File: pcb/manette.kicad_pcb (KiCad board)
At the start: 2 copper layers, 95 x 51.5 mm, 13 parts

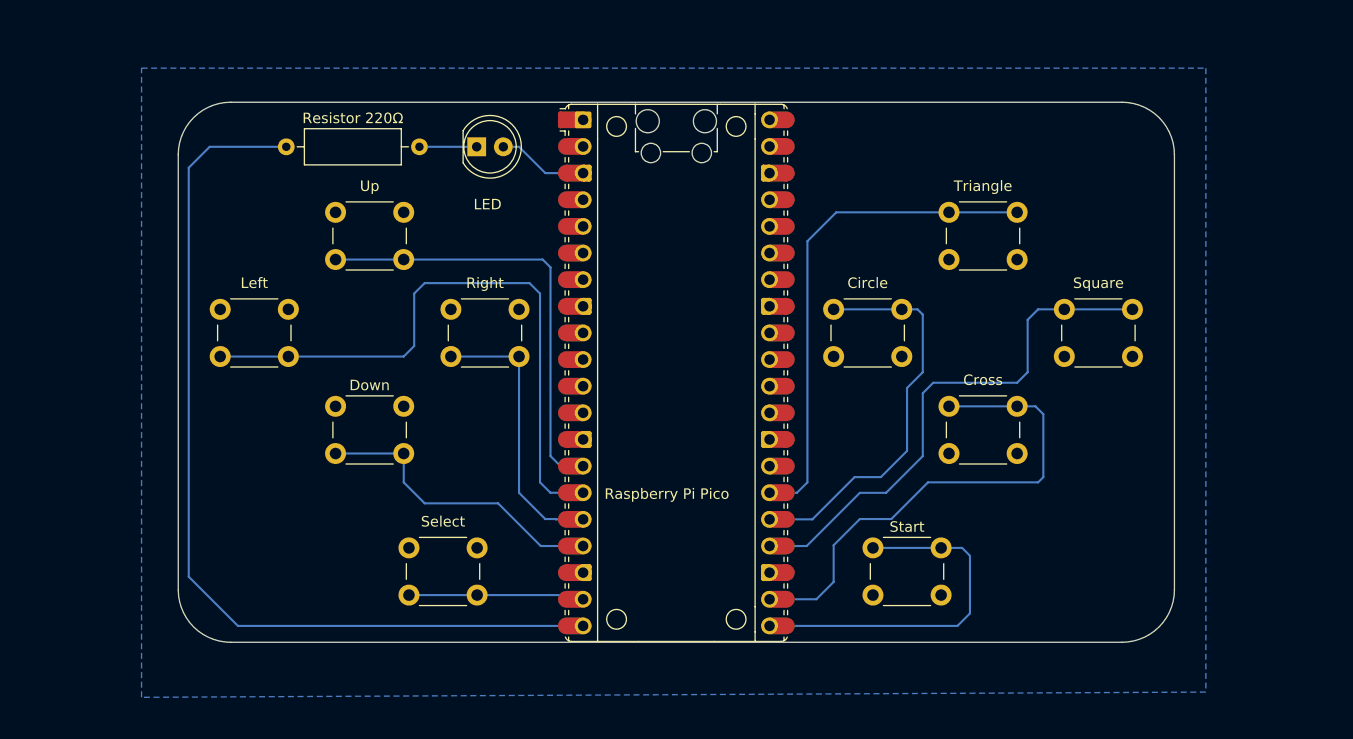
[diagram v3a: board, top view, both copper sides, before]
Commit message: ajout trous de fixation, élargissement des pistes et des pads
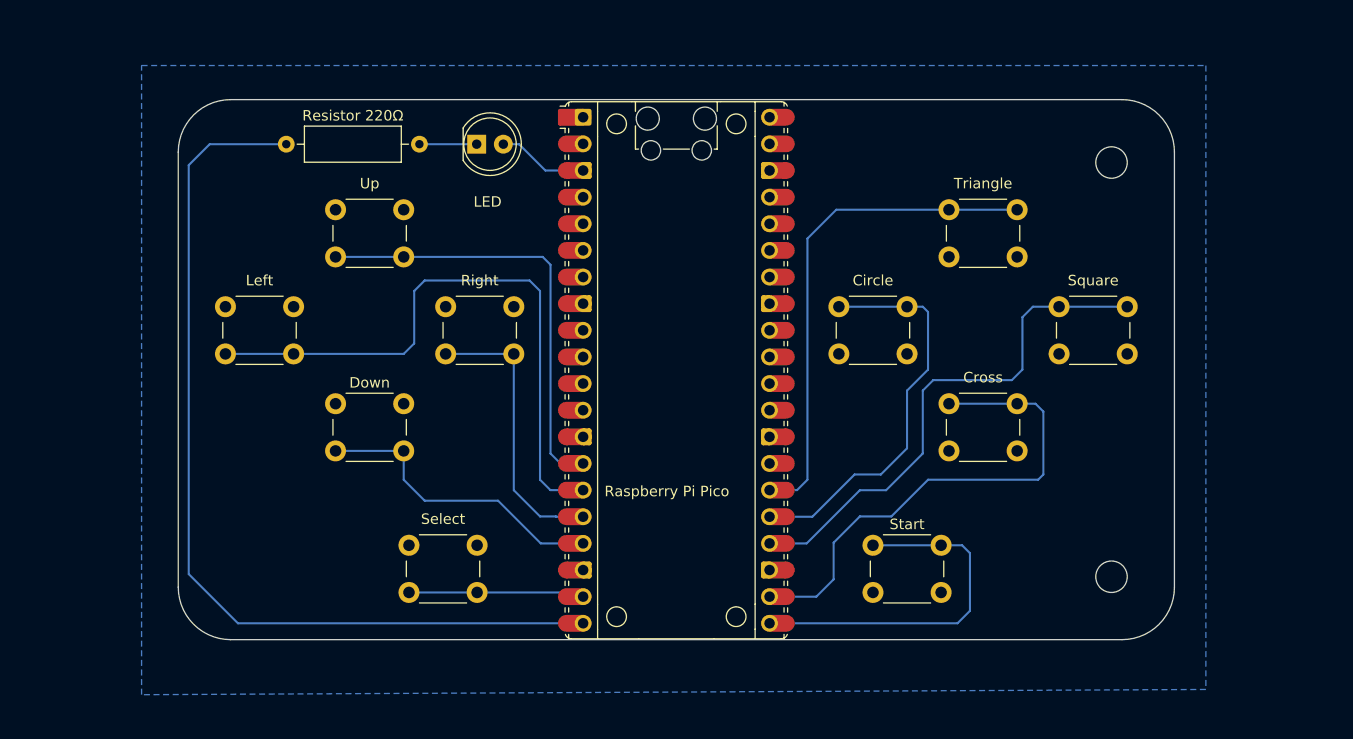
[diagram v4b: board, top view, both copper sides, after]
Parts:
- moved Circle 0.56 mm to (165.5, 98.8)
- moved Left 0.56 mm to (107.0, 98.8)
- moved Right 0.56 mm to (128.0, 98.8)
- moved Square 0.56 mm to (186.5, 98.8)
- moved Cross 0.25 mm to (176.0, 108.0)
- moved Down 0.25 mm to (117.5, 108.0)
- moved LED 0.25 mm to (131.0, 83.2)
- moved Raspberry Pi Pico 0.25 mm to (150.0, 104.8)
- moved Resistor 220Ω 0.25 mm to (112.8, 83.2)
- moved Select 0.25 mm to (124.5, 121.5)
- moved Start 0.25 mm to (168.8, 121.5)
- moved Triangle 0.25 mm to (176.0, 89.5)
- moved Up 0.25 mm to (117.5, 89.5)
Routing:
- net Net-(A1-GPIO18): track 50.4 -> 49.9 mm
- net Net-(A1-GPIO12): track 26.7 -> 27.2 mm
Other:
- outline, holes or cut-outs redrawn

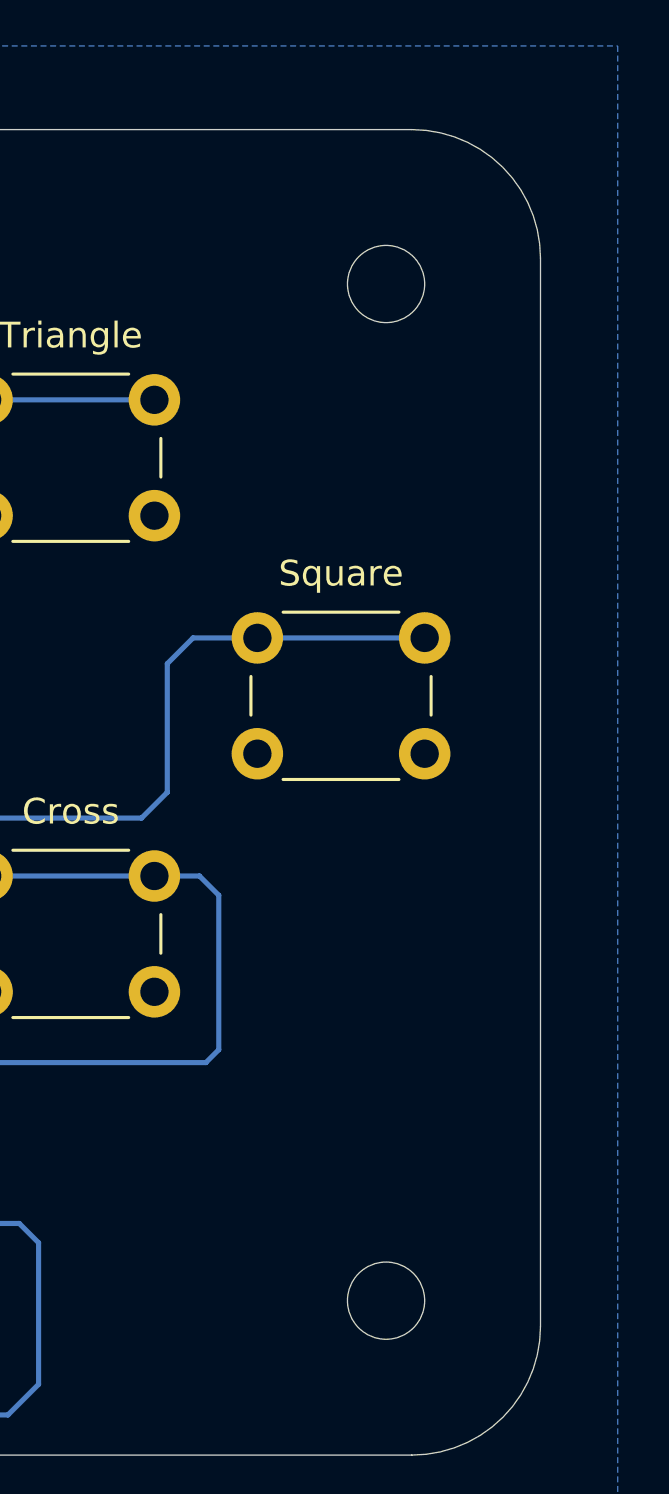
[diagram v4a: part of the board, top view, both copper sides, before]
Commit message: replaced edge.cut holes with footprint drill holes
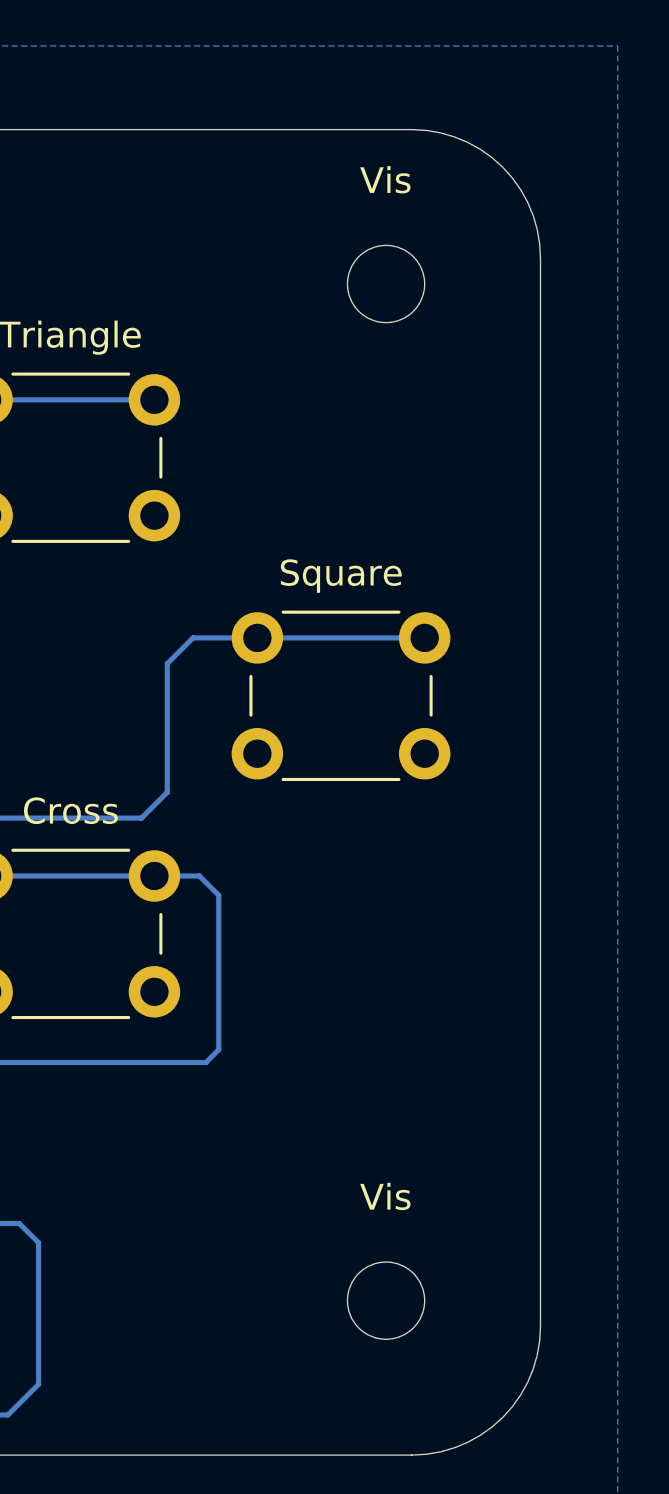
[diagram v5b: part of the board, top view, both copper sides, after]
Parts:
- added Vis: MountingHole_3mm, MountingHole:MountingHole_3mm, F.Cu at (191.5, 124.5)
- added Vis: MountingHole_3mm, MountingHole:MountingHole_3mm, F.Cu at (191.5, 85.0)
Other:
- outline, holes or cut-outs redrawn
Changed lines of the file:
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@@
 	(net 56 "unconnected-(A1-3V3_EN-Pad37)_1")
 	(net 57 "Net-(D1-K)")
+	(footprint "MountingHole:MountingHole_3mm"
+		(layer "F.Cu")
+		(at 191.5 124.5)
+		(descr "Mounting Hole 3mm, no annular")
+		(tags "mounting hole 3mm no annular")
+		(property "Reference" "Vis"
+			(at 0 -4 0)
+			(layer "F.SilkS")
+			(effects
+				(font
+					(size 1 1)
+					(thickness 0.15)
+				)
+			)
+		)
+		(property "Value" "MountingHole_3mm"
+			(at 0 4 0)
+			(layer "F.Fab")
+			(effects
+				(font
+					(size 1 1)
+					(thickness 0.15)
+				)
+			)
+		)
+		(property "Footprint" "MountingHole:MountingHole_3mm"
+			(at 0 0 0)
+			(unlocked yes)
+			(layer "F.Fab")
+			(hide yes)
+			(effects
+				(font
+					(size 1.27 1.27)
+					(thickness 0.15)
+				)
+			)
+		)
+		(property "Datasheet" ""
+			(at 0 0 0)
+			(unlocked yes)
+			(layer "F.Fab")
+			(hide yes)
+			(effects
+				(font
+					(size 1.27 1.27)
+					(thickness 0.15)
+				)
+			)
+		)
+		(property "Description" ""
+			(at 0 0 0)
+			(unlocked yes)
+			(layer "F.Fab")
+			(hide yes)
+			(effects
+				(font
+					(size 1.27 1.27)
+					(thickness 0.15)
+				)
+			)
+		)
+		(attr exclude_from_pos_files exclude_from_bom)
+		(fp_circle
+			(center 0 0)
+			(end 3 0)
+			(stroke
+				(width 0.15)
+				(type solid)
+			)
+			(fill none)
+			(layer "Cmts.User")
+		)
+		(fp_circle
+			(center 0 0)
+			(end 3.25 0)
+			(stroke
+				(width 0.05)
+				(type solid)
+			)
+			(fill none)
+			(layer "F.CrtYd")
+		)
+		(fp_text user "${REFERENCE}"
+			(at 0 0 0)
+			(layer "F.Fab")
+			(effects
+				(font
+					(size 1 1)
+					(thickness 0.15)
+				)
+			)
+		)
+		(pad "" np_thru_hole circle
+			(at 0 0)
+			(size 3 3)
+			(drill 3)
+			(layers "*.Cu" "*.Mask" "In1.Cu" "In2.Cu" "In3.Cu" "In4.Cu" "In5.Cu" "In6.Cu"
+				"In7.Cu" "In8.Cu" "In9.Cu" "In10.Cu" "In11.Cu" "In12.Cu" "In13.Cu" "In14.Cu"
+				"In15.Cu" "In16.Cu" "In17.Cu" "In18.Cu" "In19.Cu" "In20.Cu" "In21.Cu"
+				"In22.Cu" "In23.Cu" "In24.Cu" "In25.Cu" "In26.Cu" "In27.Cu" "In28.Cu"
+				"In29.Cu" "In30.Cu"
+			)
+		)
+	)
 	(footprint "Button_Switch_THT:SW_PUSH_6mm_H4.3mm"
 		(layer "F.Cu")
@@
 		)
 	)
+	(footprint "MountingHole:MountingHole_3mm"
+		(layer "F.Cu")
+		(at 191.5 85)
+		(descr "Mounting Hole 3mm, no annular")
+		(tags "mounting hole 3mm no annular")
+		(property "Reference" "Vis"
+			(at 0 -4 0)
+			(layer "F.SilkS")
+			(effects
+				(font
+					(size 1 1)
+					(thickness 0.15)
+				)
+			)
+		)
+		(property "Value" "MountingHole_3mm"
+			(at 0 4 0)
+			(layer "F.Fab")
+			(effects
+				(font
+					(size 1 1)
+					(thickness 0.15)
+				)
+			)
+		)
+		(property "Footprint" "MountingHole:MountingHole_3mm"
+			(at 0 0 0)
+			(unlocked yes)
+			(layer "F.Fab")
+			(hide yes)
+			(effects
+				(font
+					(size 1.27 1.27)
+					(thickness 0.15)
+				)
+			)
+		)
+		(property "Datasheet" ""
+			(at 0 0 0)
+			(unlocked yes)
+			(layer "F.Fab")
+			(hide yes)
+			(effects
+				(font
+					(size 1.27 1.27)
+					(thickness 0.15)
+				)
+			)
+		)
+		(property "Description" ""
+			(at 0 0 0)
+			(unlocked yes)
+			(layer "F.Fab")
+			(hide yes)
+			(effects
+				(font
+					(size 1.27 1.27)
+					(thickness 0.15)
+				)
+			)
+		)
+		(attr exclude_from_pos_files exclude_from_bom)
+		(fp_circle
+			(center 0 0)
+			(end 3 0)
+			(stroke
+				(width 0.15)
+				(type solid)
+			)
+			(fill none)
+			(layer "Cmts.User")
+		)
+		(fp_circle
+			(center 0 0)
+			(end 3.25 0)
+			(stroke
+				(width 0.05)
+				(type solid)
+			)
+			(fill none)
+			(layer "F.CrtYd")
+		)
+		(fp_text user "${REFERENCE}"
+			(at 0 0 0)
+			(layer "F.Fab")
+			(effects
+				(font
+					(size 1 1)
+					(thickness 0.15)
+				)
+			)
+		)
+		(pad "" np_thru_hole circle
+			(at 0 0)
+			(size 3 3)
+			(drill 3)
+			(layers "*.Cu" "*.Mask" "In1.Cu" "In2.Cu" "In3.Cu" "In4.Cu" "In5.Cu" "In6.Cu"
+				"In7.Cu" "In8.Cu" "In9.Cu" "In10.Cu" "In11.Cu" "In12.Cu" "In13.Cu" "In14.Cu"
+				"In15.Cu" "In16.Cu" "In17.Cu" "In18.Cu" "In19.Cu" "In20.Cu" "In21.Cu"
+				"In22.Cu" "In23.Cu" "In24.Cu" "In25.Cu" "In26.Cu" "In27.Cu" "In28.Cu"
+				"In29.Cu" "In30.Cu"
+			)
+		)
+	)
 	(footprint "Button_Switch_THT:SW_PUSH_6mm_H4.3mm"
 		(layer "F.Cu")
@@
 		(tags "Resistor Axial_DIN0309 series Axial Horizontal pin pitch 12.7mm 0.5W = 1/2W length 9mm diameter 3.2mm")
 		(property "Reference" "Resistor 220Ω"
-			(at 6.35 -2.72 360)
+			(at 6.35 -2.72 0)
 			(layer "F.SilkS")
 			(effects
@@
 		)
 		(property "Value" "220Ω"
-			(at 6.35 2.72 360)
+			(at 6.35 2.72 0)
 			(layer "F.Fab")
 			(effects
@@
 		)
 		(fp_text user "${REFERENCE}"
-			(at 6.35 0 360)
+			(at 6.35 0 0)
 			(layer "F.Fab")
 			(effects
@@
 		(tags "LED")
 		(property "Reference" "LED"
-			(at 1.04 5.5 360)
+			(at 1.04 5.5 0)
 			(layer "F.SilkS")
 			(effects
@@
 		)
 		(property "Value" "Blue"
-			(at 1.27 3.96 360)
+			(at 1.27 3.96 0)
 			(layer "F.Fab")
 			(effects
@@
 		)
 		(property "Footprint" "LED_THT:LED_D5.0mm"
-			(at 0 0 360)
+			(at 0 0 0)
 			(layer "F.Fab")
 			(hide yes)
@@
 		)
 		(property "Datasheet" ""
-			(at 0 0 360)
+			(at 0 0 0)
 			(layer "F.Fab")
 			(hide yes)
@@
 		)
 		(property "Description" "Light emitting diode"
-			(at 0 0 360)
+			(at 0 0 0)
 			(layer "F.Fab")
 			(hide yes)
@@
 		)
 		(fp_text user "${REFERENCE}"
-			(at 1.27 0 360)
+			(at 1.27 0 0)
 			(layer "F.Fab")
 			(effects
@@
 		)
 	)
-	(gr_circle
-		(center 191.5 124.5)
-		(end 193 124.5)
-		(stroke
-			(width 0.05)
-			(type default)
-		)
-		(fill none)
-		(layer "Edge.Cuts")
-	)
 	(gr_arc
 		(start 107.5 130.5)
@@
 		(layer "Edge.Cuts")
 	)
-	(gr_circle
-		(center 191.5 85)
-		(end 193 85)
-		(stroke
-			(width 0.05)
-			(type default)
-		)
-		(fill none)
-		(layer "Edge.Cuts")
-	)

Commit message: fixed design constraints and rolled back to edge.cut holes
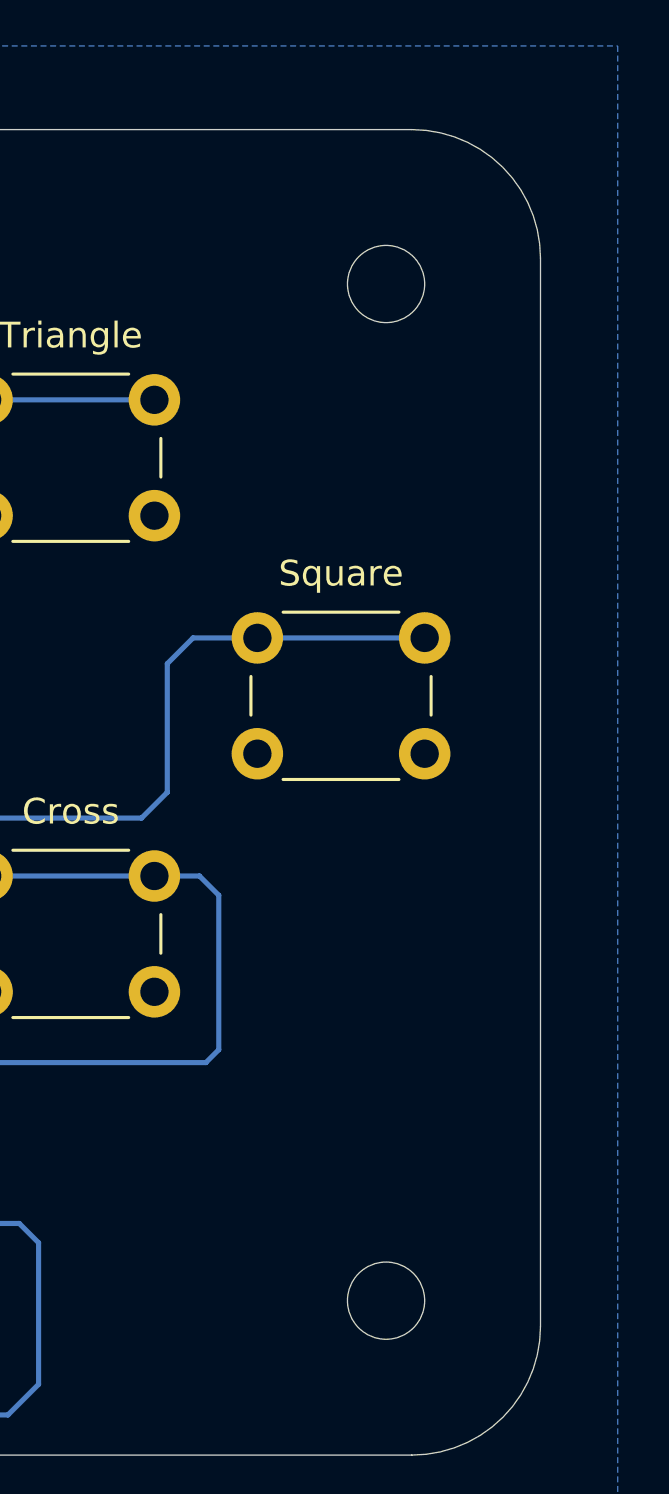
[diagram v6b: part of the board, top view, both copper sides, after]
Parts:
- removed Vis (x2): MountingHole_3mm, MountingHole:MountingHole_3mm
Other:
- outline, holes or cut-outs redrawn
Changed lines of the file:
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@@
 	(net 56 "unconnected-(A1-3V3_EN-Pad37)_1")
 	(net 57 "Net-(D1-K)")
-	(footprint "MountingHole:MountingHole_3mm"
-		(layer "F.Cu")
-		(at 191.5 124.5)
-		(descr "Mounting Hole 3mm, no annular")
-		(tags "mounting hole 3mm no annular")
-		(property "Reference" "Vis"
-			(at 0 -4 0)
-			(layer "F.SilkS")
-			(effects
-				(font
-					(size 1 1)
-					(thickness 0.15)
-				)
-			)
-		)
-		(property "Value" "MountingHole_3mm"
-			(at 0 4 0)
-			(layer "F.Fab")
-			(effects
-				(font
-					(size 1 1)
-					(thickness 0.15)
-				)
-			)
-		)
-		(property "Footprint" "MountingHole:MountingHole_3mm"
-			(at 0 0 0)
-			(unlocked yes)
-			(layer "F.Fab")
-			(hide yes)
-			(effects
-				(font
-					(size 1.27 1.27)
-					(thickness 0.15)
-				)
-			)
-		)
-		(property "Datasheet" ""
-			(at 0 0 0)
-			(unlocked yes)
-			(layer "F.Fab")
-			(hide yes)
-			(effects
-				(font
-					(size 1.27 1.27)
-					(thickness 0.15)
-				)
-			)
-		)
-		(property "Description" ""
-			(at 0 0 0)
-			(unlocked yes)
-			(layer "F.Fab")
-			(hide yes)
-			(effects
-				(font
-					(size 1.27 1.27)
-					(thickness 0.15)
-				)
-			)
-		)
-		(attr exclude_from_pos_files exclude_from_bom)
-		(fp_circle
-			(center 0 0)
-			(end 3 0)
-			(stroke
-				(width 0.15)
-				(type solid)
-			)
-			(fill none)
-			(layer "Cmts.User")
-		)
-		(fp_circle
-			(center 0 0)
-			(end 3.25 0)
-			(stroke
-				(width 0.05)
-				(type solid)
-			)
-			(fill none)
-			(layer "F.CrtYd")
-		)
-		(fp_text user "${REFERENCE}"
-			(at 0 0 0)
-			(layer "F.Fab")
-			(effects
-				(font
-					(size 1 1)
-					(thickness 0.15)
-				)
-			)
-		)
-		(pad "" np_thru_hole circle
-			(at 0 0)
-			(size 3 3)
-			(drill 3)
-			(layers "*.Cu" "*.Mask" "In1.Cu" "In2.Cu" "In3.Cu" "In4.Cu" "In5.Cu" "In6.Cu"
-				"In7.Cu" "In8.Cu" "In9.Cu" "In10.Cu" "In11.Cu" "In12.Cu" "In13.Cu" "In14.Cu"
-				"In15.Cu" "In16.Cu" "In17.Cu" "In18.Cu" "In19.Cu" "In20.Cu" "In21.Cu"
-				"In22.Cu" "In23.Cu" "In24.Cu" "In25.Cu" "In26.Cu" "In27.Cu" "In28.Cu"
-				"In29.Cu" "In30.Cu"
-			)
-		)
-	)
 	(footprint "Button_Switch_THT:SW_PUSH_6mm_H4.3mm"
 		(layer "F.Cu")
@@
 		)
 	)
-	(footprint "MountingHole:MountingHole_3mm"
-		(layer "F.Cu")
-		(at 191.5 85)
-		(descr "Mounting Hole 3mm, no annular")
-		(tags "mounting hole 3mm no annular")
-		(property "Reference" "Vis"
-			(at 0 -4 0)
-			(layer "F.SilkS")
-			(effects
-				(font
-					(size 1 1)
-					(thickness 0.15)
-				)
-			)
-		)
-		(property "Value" "MountingHole_3mm"
-			(at 0 4 0)
-			(layer "F.Fab")
-			(effects
-				(font
-					(size 1 1)
-					(thickness 0.15)
-				)
-			)
-		)
-		(property "Footprint" "MountingHole:MountingHole_3mm"
-			(at 0 0 0)
-			(unlocked yes)
-			(layer "F.Fab")
-			(hide yes)
-			(effects
-				(font
-					(size 1.27 1.27)
-					(thickness 0.15)
-				)
-			)
-		)
-		(property "Datasheet" ""
-			(at 0 0 0)
-			(unlocked yes)
-			(layer "F.Fab")
-			(hide yes)
-			(effects
-				(font
-					(size 1.27 1.27)
-					(thickness 0.15)
-				)
-			)
-		)
-		(property "Description" ""
-			(at 0 0 0)
-			(unlocked yes)
-			(layer "F.Fab")
-			(hide yes)
-			(effects
-				(font
-					(size 1.27 1.27)
-					(thickness 0.15)
-				)
-			)
-		)
-		(attr exclude_from_pos_files exclude_from_bom)
-		(fp_circle
-			(center 0 0)
-			(end 3 0)
-			(stroke
-				(width 0.15)
-				(type solid)
-			)
-			(fill none)
-			(layer "Cmts.User")
-		)
-		(fp_circle
-			(center 0 0)
-			(end 3.25 0)
-			(stroke
-				(width 0.05)
-				(type solid)
-			)
-			(fill none)
-			(layer "F.CrtYd")
-		)
-		(fp_text user "${REFERENCE}"
-			(at 0 0 0)
-			(layer "F.Fab")
-			(effects
-				(font
-					(size 1 1)
-					(thickness 0.15)
-				)
-			)
-		)
-		(pad "" np_thru_hole circle
-			(at 0 0)
-			(size 3 3)
-			(drill 3)
-			(layers "*.Cu" "*.Mask" "In1.Cu" "In2.Cu" "In3.Cu" "In4.Cu" "In5.Cu" "In6.Cu"
-				"In7.Cu" "In8.Cu" "In9.Cu" "In10.Cu" "In11.Cu" "In12.Cu" "In13.Cu" "In14.Cu"
-				"In15.Cu" "In16.Cu" "In17.Cu" "In18.Cu" "In19.Cu" "In20.Cu" "In21.Cu"
-				"In22.Cu" "In23.Cu" "In24.Cu" "In25.Cu" "In26.Cu" "In27.Cu" "In28.Cu"
-				"In29.Cu" "In30.Cu"
-			)
-		)
-	)
 	(footprint "Button_Switch_THT:SW_PUSH_6mm_H4.3mm"
 		(layer "F.Cu")
@@
 		)
 	)
+	(gr_circle
+		(center 191.5 85)
+		(end 193 85)
+		(stroke
+			(width 0.05)
+			(type default)
+		)
+		(fill none)
+		(layer "Edge.Cuts")
+	)
 	(gr_arc
 		(start 107.5 130.5)
@@
 		(layer "Edge.Cuts")
 	)
+	(gr_circle
+		(center 191.5 124.5)
+		(end 193 124.5)
+		(stroke
+			(width 0.05)
+			(type default)
+		)
+		(fill none)
+		(layer "Edge.Cuts")
+	)
